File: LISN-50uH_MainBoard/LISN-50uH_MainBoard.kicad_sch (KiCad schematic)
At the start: 76 parts, among them J1 Conn_Coaxial, J2 Conn_Coaxial, J3 Conn_01x01_Pin, J4 Conn_01x01_Pin, J5 Conn_01x01_Pin, J6 Conn_01x01_Pin

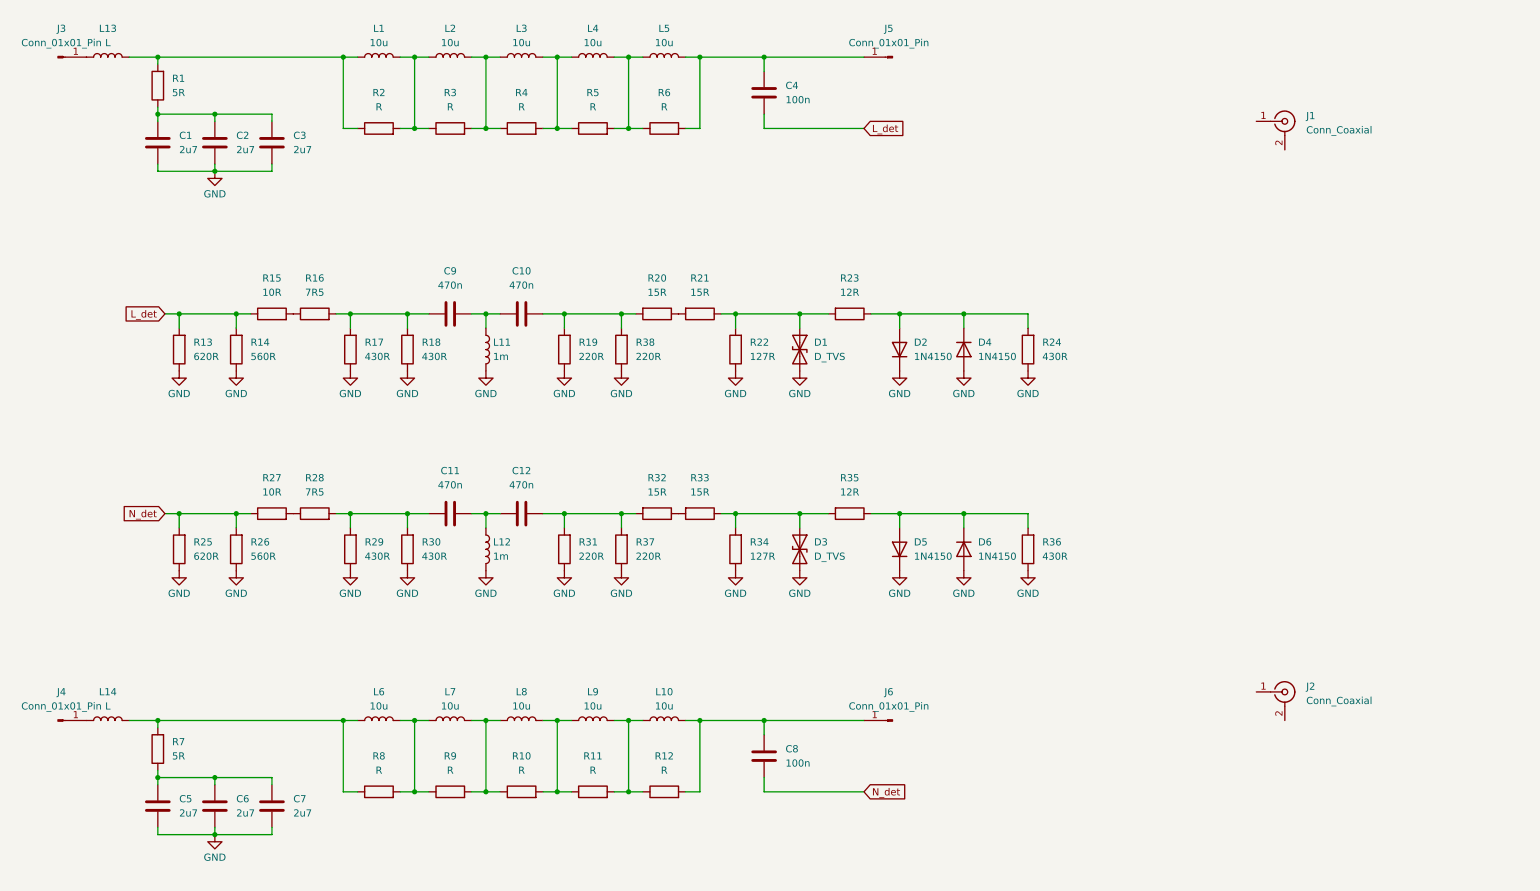
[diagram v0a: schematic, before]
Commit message: sch update - changes in filter path. pcb - change PCB dimensions
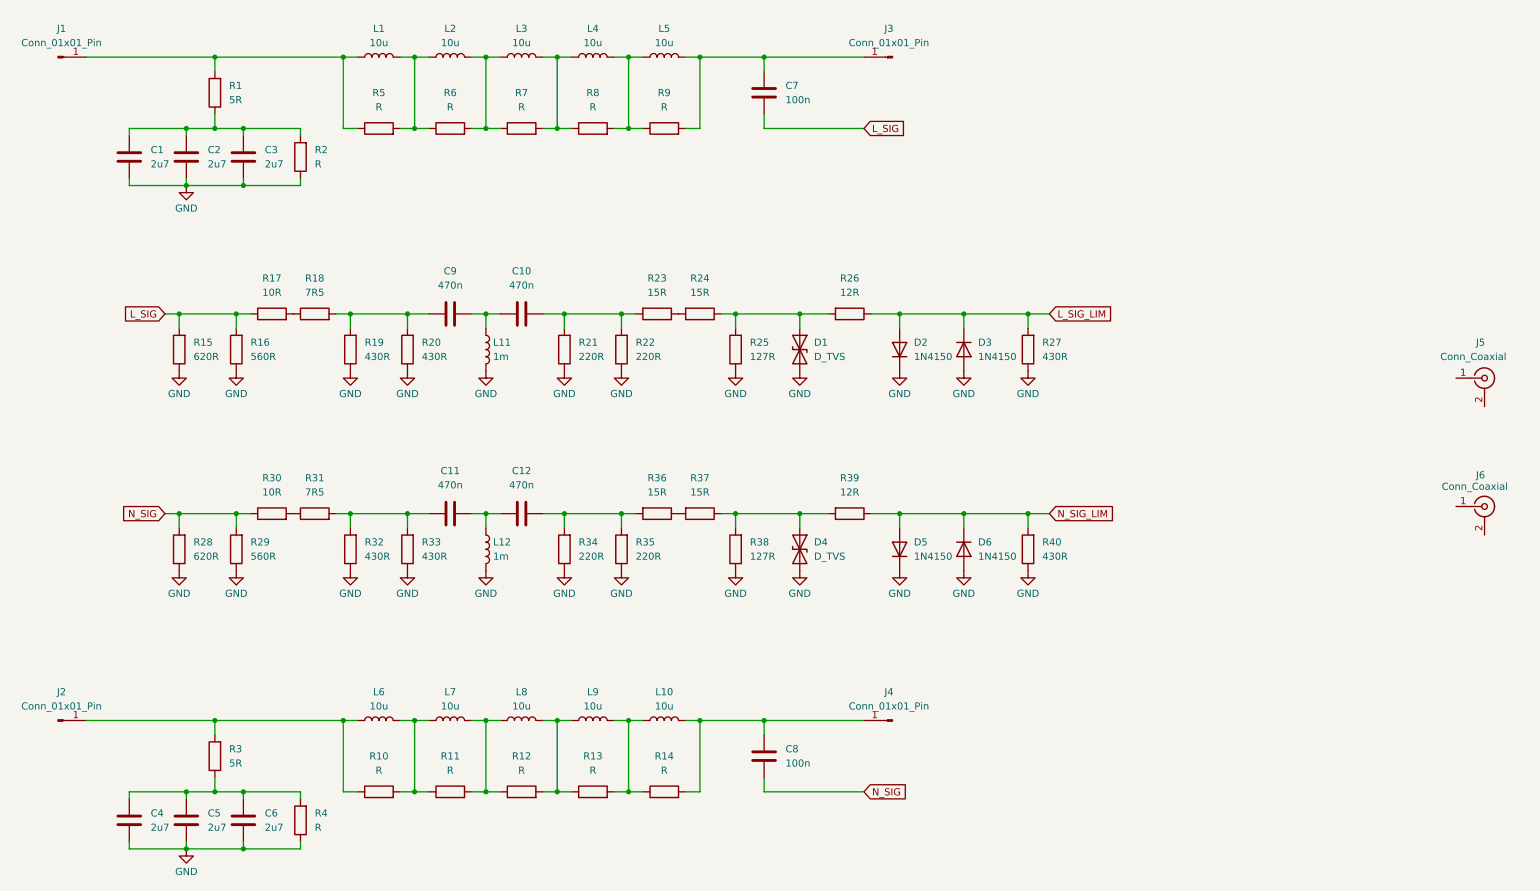
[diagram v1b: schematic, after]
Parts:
- removed L13, L14: L, Inductor_THT:L_Toroid_Vertical_L10.0mm_W5.0mm_P5.08mm, symbol Device:L
- added R2, R4: R, Resistor_SMD:R_2010_5025Metric, symbol Device:R
- renumbered C5 to C4, C6 to C5, C7 to C6, C4 to C7, D4 to D3, D3 to D4, J3 to J1, J4 to J2, J5 to J3, J6 to J4, J1 to J5, J2 to J6, R8 to R10, R9 to R11, R10 to R12, R11 to R13, R12 to R14, R13 to R15, R14 to R16, R15 to R17, R16 to R18, R17 to R19, R18 to R20, R19 to R21, R38 to R22, R20 to R23, R21 to R24, R22 to R25, R23 to R26, R24 to R27, R25 to R28, R26 to R29, R7 to R3, R27 to R30, R28 to R31, R29 to R32, R30 to R33, R31 to R34, R37 to R35, R32 to R36, R33 to R37, R34 to R38, R35 to R39, R36 to R40, R2 to R5, R3 to R6, R4 to R7, R5 to R8, R6 to R9
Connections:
- net GND: now also R2.1, R4.1
- net at L1.1, R1.2, R5.1: now also J1.1 (Pin_1)
- net N_SIG_LIM: now reaches D5.2 (A), D6.1 (K), R39.1, R40.2
- net at C4.1, C5.1, C6.1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: now also R4.2
- net at L6.1, R10.1, R3.2: now also J2.1 (Pin_1)
- net L_SIG_LIM: now reaches D2.2 (A), D3.1 (K), R26.1, R27.2
- net at C1.1, C2.1, C3.1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: now also R2.2
- net L_det renamed L_SIG
- net N_det renamed N_SIG
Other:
- moved on the sheet: C1, C2, C3, C4, C5, C6, J5, J6, R1, R3

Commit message: changes in low pass filter/limiter path
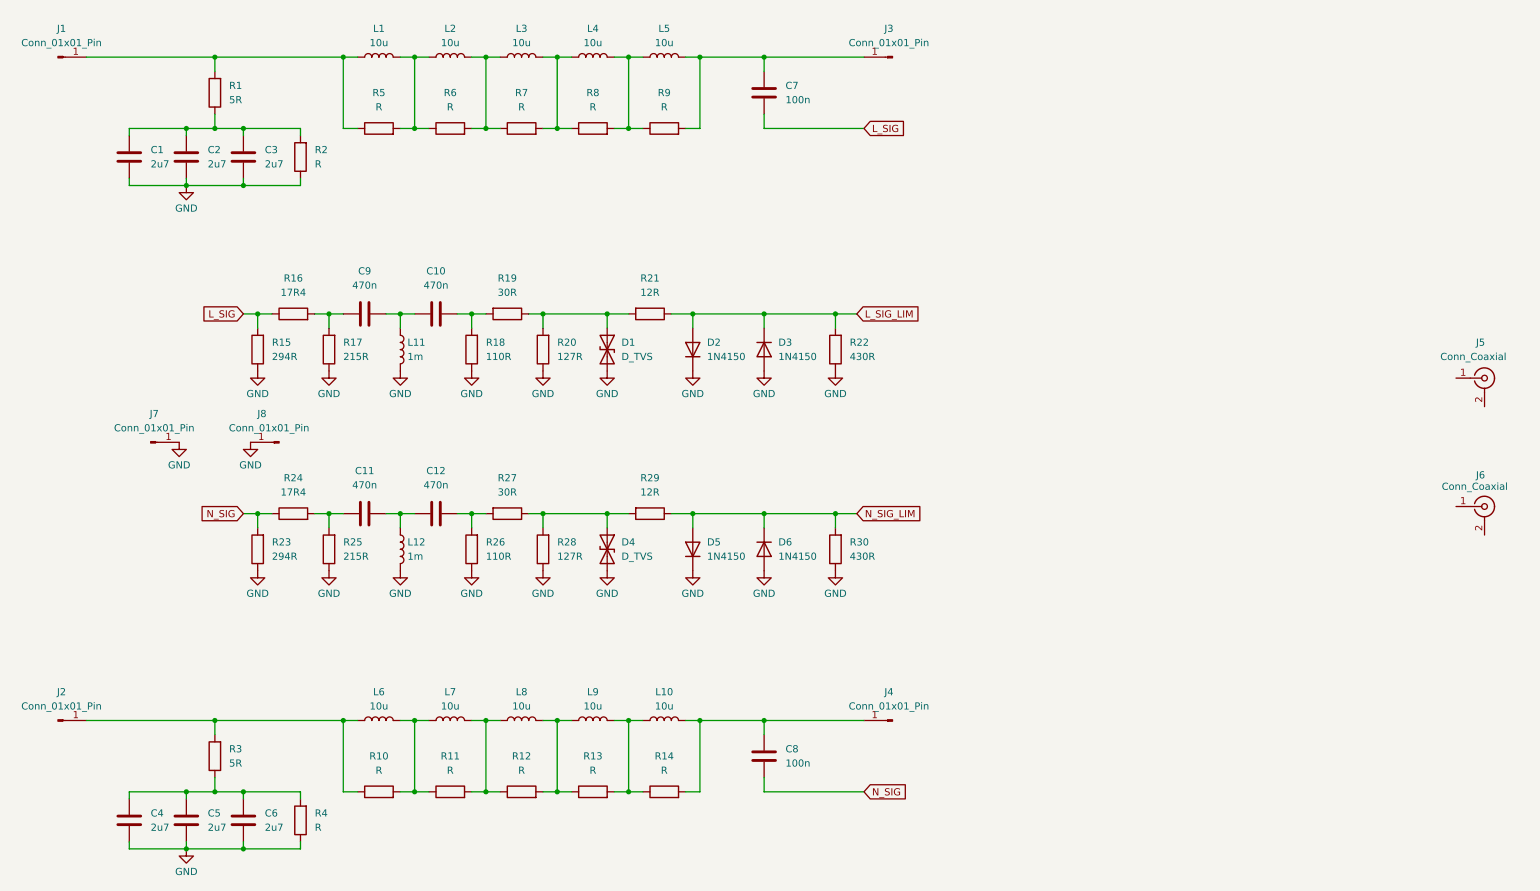
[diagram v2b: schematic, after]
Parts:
- removed R16, R29: 560R, Resistor_SMD:R_0805_2012Metric, symbol Device:R
- removed R18, R31: 7R5, Resistor_SMD:R_0805_2012Metric, symbol Device:R
- removed R20, R33: 430R, Resistor_SMD:R_0805_2012Metric, symbol Device:R
- removed R22, R35: 220R, Resistor_SMD:R_0805_2012Metric, symbol Device:R
- removed R24, R37: 15R, Resistor_SMD:R_0805_2012Metric, symbol Device:R
- added J7, J8: Conn_01x01_Pin, a_project_library:Faston_Tab_6.3x0.8, symbol Connector:Conn_01x01_Pin
- R15: value 620R -> 294R
- R16: renamed from R17; value 10R -> 17R4
- R17: renamed from R19; value 430R -> 215R
- R18: renamed from R21; value 220R -> 110R
- R19: renamed from R23; value 15R -> 30R
- R23: renamed from R28; value 620R -> 294R
- R24: renamed from R30; value 10R -> 17R4
- R25: renamed from R32; value 430R -> 215R
- R26: renamed from R34; value 220R -> 110R
- R27: renamed from R36; value 15R -> 30R
- renumbered R25 to R20, R26 to R21, R27 to R22, R38 to R28, R39 to R29, R40 to R30
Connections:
- net GND: now also J7.1 (Pin_1), J8.1 (Pin_1)
- net at R16.2: now also C9.1, R17.2
- net at R27.1: now also D4.1 (A1), R28.2, R29.2
- net at R24.2: now also C11.1, R25.2
- net at D1.1 (A1), R20.2, R21.2: now also R19.1
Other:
- moved on the sheet: C10, C11, C12, C9, D1, D2, D3, D4, D5, D6, L11, L12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

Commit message: sch - add GDT and optional input toroidal line choke pcb - routing in progress
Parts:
- added GD1, GD2: GDT_2Pin, a_project_library:GDT_D8_P10.16_Horizontal, symbol Device:GDT_2Pin
- added L13, L14: L, Inductor_THT:L_Toroid_Vertical_L13.0mm_W6.5mm_P5.60mm, symbol Device:L
- added R31, R33, R36: DNP, Resistor_SMD:R_0805_2012Metric, symbol Device:R
- added R32: 0, Resistor_SMD:R_0805_2012Metric, symbol Device:R
- added R34: 50R, Resistor_SMD:R_0805_2012Metric, symbol Device:R
- added R35: 0R, Resistor_SMD:R_0805_2012Metric, symbol Device:R
- J1, J2, J3, J4, J7, J8: value Conn_01x01_Pin -> Faston Tab 6.3mm
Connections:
- net GND: now also J5.2 (Ext), J6.2 (Ext), GD1.1, GD2.1, R31.1, R33.1, R34.1, R36.1
- net L_SIG: now also GD1.3
- net N_SIG: now also GD2.3
- net L_l: now reaches L1.1, R1.2, R5.1
- net L_l: now also L13.2; no longer J1.1 (Pin_1)
- net L_l1: now reaches L1.2, L2.1, R5.2, R6.1
- net N_C: now reaches C4.1, C5.1, C6.1, R3.1, R4.2
- net N_l: now reaches L6.1, R10.1, R3.2
- net N_l: now also L14.2; no longer J2.1 (Pin_1)
- net at J5.1 (In): now also R32.1, R33.2
- net N_l3: now reaches L8.2, L9.1, R12.2, R13.1
- net N_l4: now reaches L10.1, L9.2, R13.2, R14.1
- net N_dut: now reaches C8.1, J4.1 (Pin_1), L10.2, R14.2
- net L_l2: now reaches L2.2, L3.1, R6.2, R7.1
- net L_l3: now reaches L3.2, L4.1, R7.2, R8.1
- net N_l2: now reaches L7.2, L8.1, R11.2, R12.1
- net L_l4: now reaches L4.2, L5.1, R8.2, R9.1
- net L_dut: now reaches C7.1, J3.1 (Pin_1), L5.2, R9.2
- net N_l1: now reaches L6.2, L7.1, R10.2, R11.1
- net L_C: now reaches C1.1, C2.1, C3.1, R1.1, R2.2
- net at J6.1 (In): now also R35.1, R36.2
- new net: R31.2, R32.2
- new net: R34.2, R35.2
- new net L_in: J1.1 (Pin_1), L13.1
- new net N_in: J2.1 (Pin_1), L14.1
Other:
- moved on the sheet: J5, J6, J8

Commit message: change input coil footprint, add RF transformer for CM/DM
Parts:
- added R37: 50R, Resistor_SMD:R_0805_2012Metric, symbol Device:R
- added TR1: ADT1-6T, RF_Mini-Circuits:Mini-Circuits_CD637_H5.23mm, symbol Transformer:ADT1-6T
- C7, C8: footprint Capacitor_THT:C_Rect_L24.0mm_W10.1mm_P22.50mm_MKT -> Capacitor_THT:C_Rect_L19.0mm_W11.0mm_P15.00mm_MKS4
- J1, J2, J3, J4, J7, J8: value Faston Tab 6.3mm -> Faston Tab 4.8mm; footprint a_project_library:Faston_Tab_6.3x0.8 -> a_project_library:Faston_Tab_4.8x0.8
- L13, L14: value L -> 250uH optional; footprint Inductor_THT:L_Toroid_Vertical_L13.0mm_W6.5mm_P5.60mm -> a_project_library:L_Toroid_Vertical_L26.0mm_W12.9mm_P10.0mm_Wuerth_WE-FI
- R34: value 50R -> DNP
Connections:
- net GND: now also R37.2, TR1.1
- net L_SIG_LIM: now also TR1.4
- net N_SIG_LIM: now also TR1.6
- net SIG_DM_out: now reaches J5.1 (In), R32.1, R33.2
- net SIG_DM: now reaches R31.2, R32.2
- net SIG_DM: now also TR1.3
- net SIG_CM: now reaches R34.2, R35.2
- net SIG_CM: now also R37.1, TR1.5
- net SIG_CM_out: now reaches J6.1 (In), R35.1, R36.2
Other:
- moved on the sheet: R31, R34

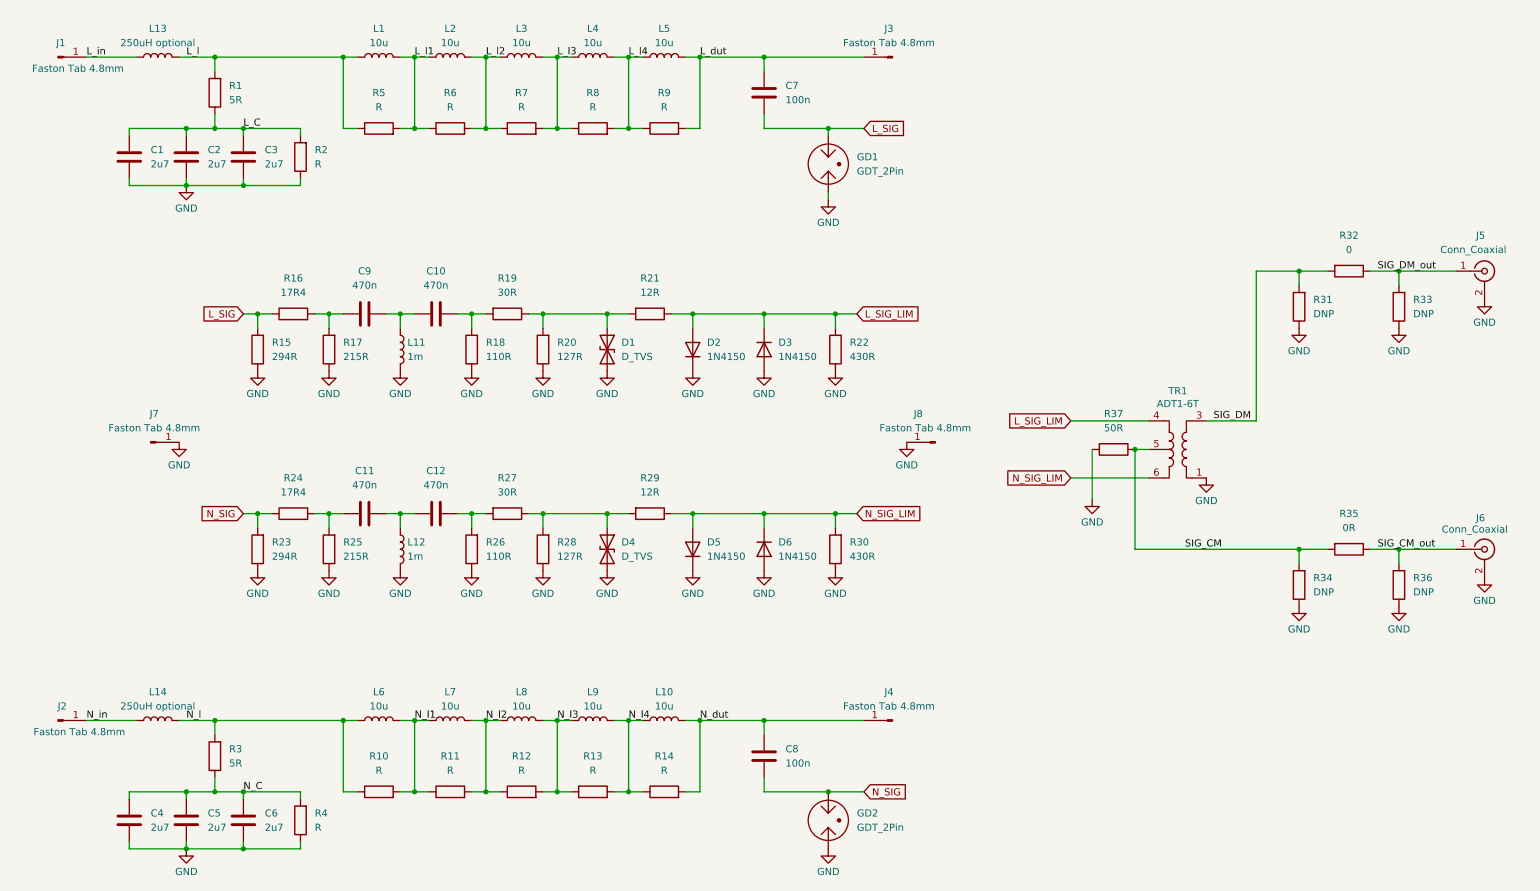
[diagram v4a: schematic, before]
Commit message: add L&N/CM&DM switch
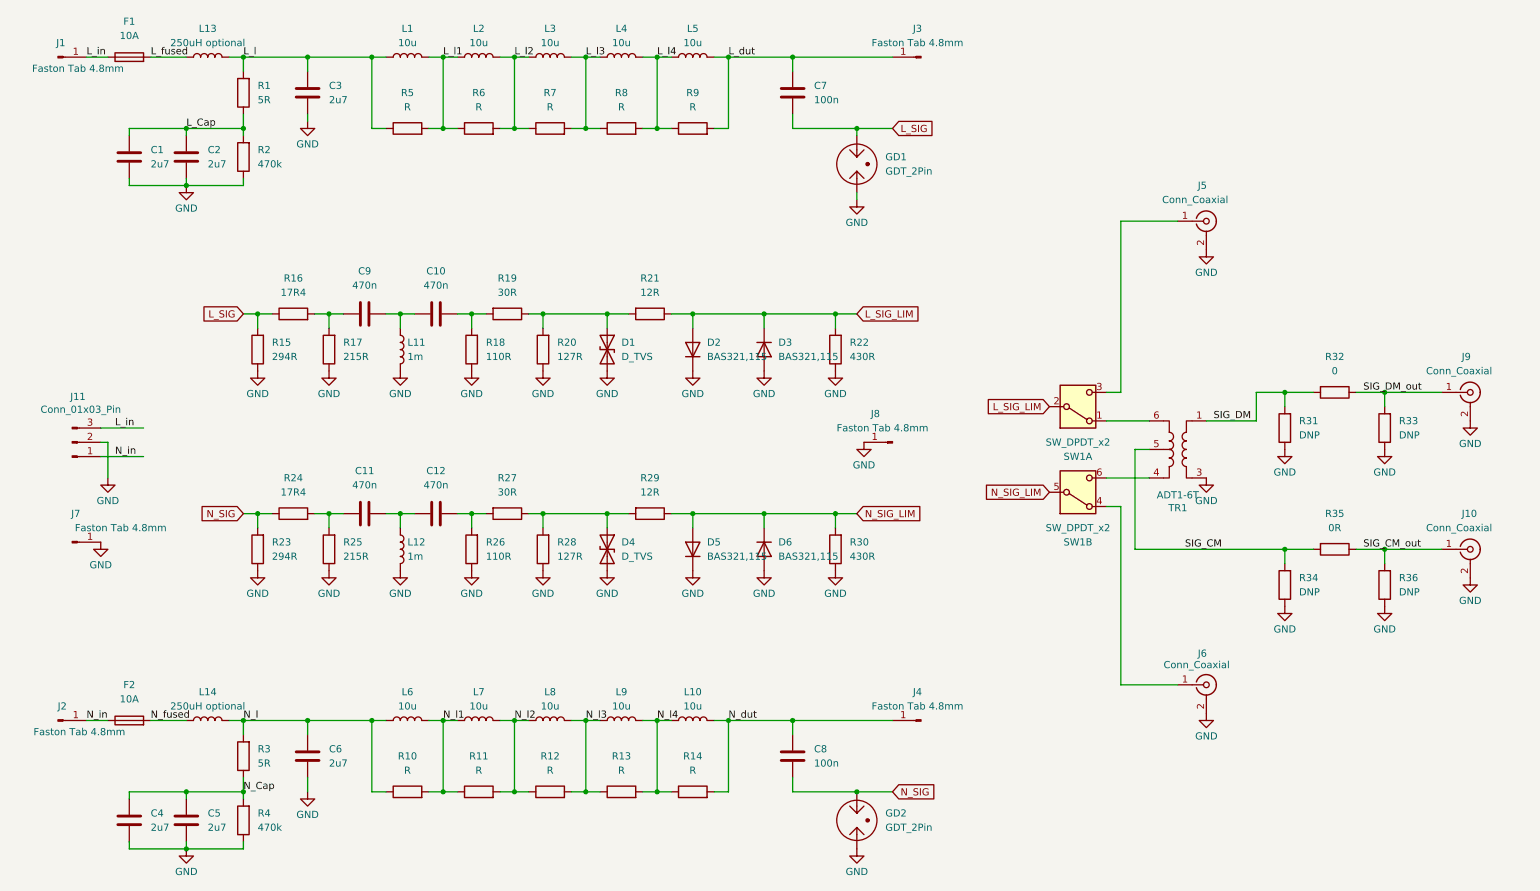
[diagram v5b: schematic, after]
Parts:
- removed R37: 50R, Resistor_SMD:R_0805_2012Metric, symbol Device:R
- added F1, F2: 10A, a_project_library:Fuseholder_Clip-5x20mm_Littelfuse_100_111_dual_Horizontal, symbol Device:Fuse
- added J10, J9: Conn_Coaxial, Connector_Coaxial:U.FL_Molex_MCRF_73412-0110_Vertical, symbol Connector:Conn_Coaxial
- added J11: Conn_01x03_Pin, a_project_library:AC_Connector_Adam_tech_IEC-A-4, symbol Connector:Conn_01x03_Pin
- added SW1: SW_DPDT_x2, a_project_library:SW_E-SWITCH_LC2255EENP_DPDT_right_angle, symbol Switch:SW_DPDT_x2
- D2, D3, D5, D6: value 1N4150 -> BAS321,115; footprint Diode_SMD:D_SOD-123 -> Diode_SMD:D_SOD-323
- L13, L14: footprint a_project_library:L_Toroid_Vertical_L26.0mm_W12.9mm_P10.0mm_Wuerth_WE-FI -> a_project_library:L_Toroid_Vertical_L38.0mm_W16.0mm_P15.0mm_Wuerth_WE-FI
- R2, R4: value R -> 470k
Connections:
- net GND: now also TR1.3, J10.2 (Ext), J11.2 (Pin_2), J9.2 (Ext); no longer TR1.1
- net L_SIG_LIM: now also SW1.2 (B); no longer TR1.4
- net L_in: now also F1.1, J11.3 (Pin_3); no longer L13.1
- net L_l: now also C3.1
- net N_SIG_LIM: now also SW1.5 (B); no longer TR1.6
- net N_in: now also F2.1, J11.1 (Pin_1); no longer L14.1
- net N_l: now also C6.1
- net SIG_CM_out: now also J10.1 (In); no longer J6.1 (In)
- net SIG_DM: now also TR1.1; no longer TR1.3
- net SIG_DM_out: now also J9.1 (In); no longer J5.1 (In)
- net L_C renamed L_Cap
- net L_Cap: no longer C3.1
- net N_C renamed N_Cap
- net N_Cap: no longer C6.1
- new net: J6.1 (In), SW1.4 (A)
- new net: SW1.6 (C), TR1.4
- new net: J5.1 (In), SW1.3 (C)
- new net: SW1.1 (A), TR1.6
- new net L_fused: F1.2, L13.1
- new net N_fused: F2.2, L14.1
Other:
- moved on the sheet: C3, C6, C7, C8, GD1, GD2, J3, J4, J5, J6, J7, J8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
